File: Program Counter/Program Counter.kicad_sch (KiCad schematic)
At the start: 48 parts, among them J1 Conn_01x03_Pin, J4 Conn_01x08_Pin, J5 Conn_01x08_Pin, U1 74LS161, U2 74LS161, U3 74LS161, U4 74LS161

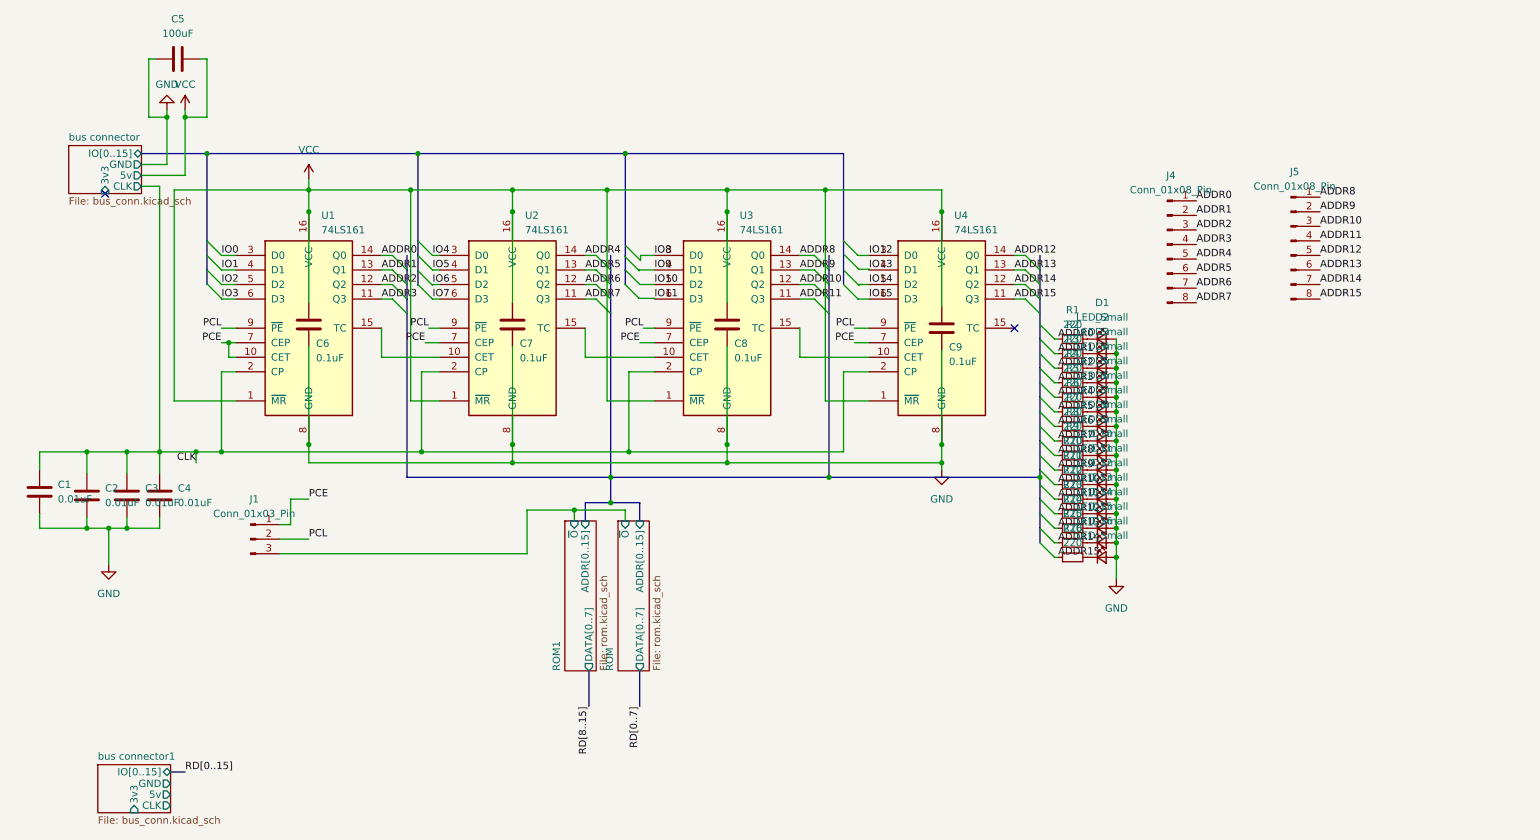
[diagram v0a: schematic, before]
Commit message: Overhauled program counter schematic
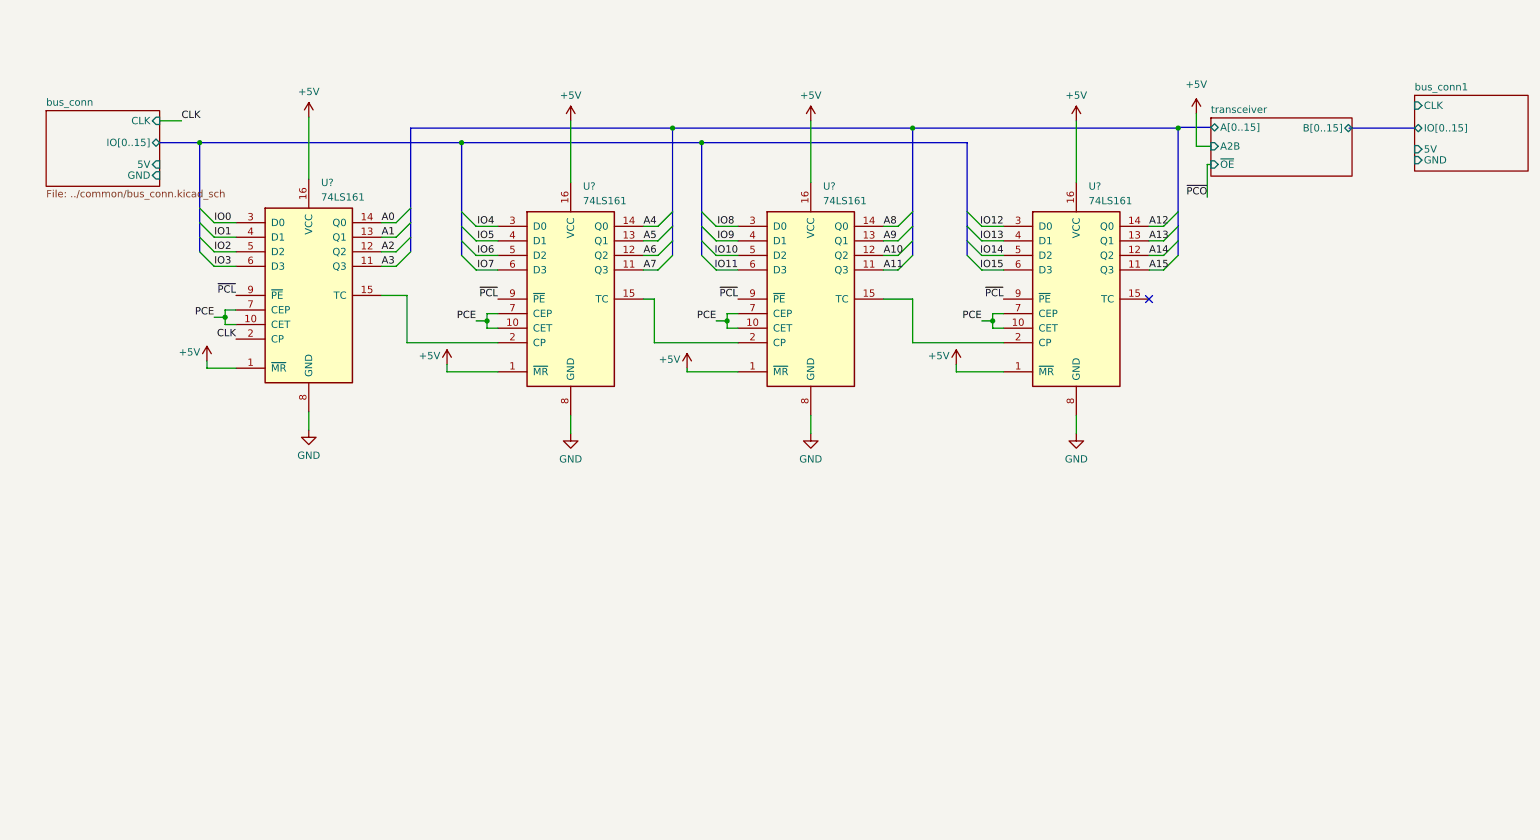
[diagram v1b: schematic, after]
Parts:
- removed C1, C2, C3, C4: 0.01uF, Capacitor_SMD:C_0603_1608Metric, symbol Device:C
- removed C5: 100uF, Capacitor_SMD:CP_Elec_5x5.3, symbol Device:C
- removed C6, C7, C8, C9: 0.1uF, Capacitor_SMD:C_0603_1608Metric, symbol Device:C
- removed D1, D10, D11, D12, D13, D14, D15, D16, D2, D3, D4, D5, D6, D7, D8, D9: LED_Small, LED_SMD:LED_0603_1608Metric, symbol Device:LED_Small
- removed J1: Conn_01x03_Pin, Connector_PinHeader_2.54mm:PinHeader_1x03_P2.54mm_Vertical, symbol Connector:Conn_01x03_Pin
- removed J4, J5: Conn_01x08_Pin, Connector_PinHeader_2.54mm:PinHeader_1x08_P2.54mm_Vertical, symbol Connector:Conn_01x08_Pin
- removed R1, R10, R11, R12, R13, R14, R15, R16, R2, R3, R4, R5, R6, R7, R8, R9: 220, Resistor_SMD:R_0603_1608Metric, symbol Device:R_Small
- removed U1, U2, U3, U4: 74LS161, Package_SO:SO-16_3.9x9.9mm_P1.27mm, symbol 74xx:74LS161
- added U? (x4): 74LS161, symbol 74xx:74LS161
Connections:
- net CLK: now also U?.2 (CP)
- net GND: now also U?.8 (GND), U?.8 (GND), U?.8 (GND), U?.8 (GND)
- net IO0: now also U?.3 (D0)
- net IO1: now also U?.4 (D1)
- net IO10: now also U?.5 (D2)
- net IO11: now also U?.6 (D3)
- net IO12: now also U?.3 (D0)
- net IO13: now also U?.4 (D1)
- net IO14: now also U?.5 (D2)
- net IO15: now also U?.6 (D3)
- net IO2: now also U?.5 (D2)
- net IO3: now also U?.6 (D3)
- net IO4: now also U?.3 (D0)
- net IO5: now also U?.4 (D1)
- net IO6: now also U?.5 (D2)
- net IO7: now also U?.6 (D3)
- net IO8: now also U?.3 (D0)
- net IO9: now also U?.4 (D1)
- net PCE: now also U?.10 (CET), U?.10 (CET), U?.10 (CET), U?.10 (CET), U?.7 (CEP), U?.7 (CEP), U?.7 (CEP), U?.7 (CEP)
- new net: U?.15 (TC), U?.2 (CP) (x3)
- new net +5V: U?.1 (~{MR}), U?.1 (~{MR}), U?.1 (~{MR}), U?.1 (~{MR}), U?.16 (VCC), U?.16 (VCC), U?.16 (VCC), U?.16 (VCC)
- new net A0: U?.14 (Q0)
- new net A1: U?.13 (Q1)
- new net A10: U?.12 (Q2)
- new net A11: U?.11 (Q3)
- new net A12: U?.14 (Q0)
- new net A13: U?.13 (Q1)
- new net A14: U?.12 (Q2)
- new net A15: U?.11 (Q3)
- new net A2: U?.12 (Q2)
- new net A3: U?.11 (Q3)
- new net A4: U?.14 (Q0)
- new net A5: U?.13 (Q1)
- new net A6: U?.12 (Q2)
- new net A7: U?.11 (Q3)
- new net A8: U?.14 (Q0)
- new net A9: U?.13 (Q1)
- new net ~{PCL}: U?.9 (~{PE}), U?.9 (~{PE}), U?.9 (~{PE}), U?.9 (~{PE})
- no-connect marks 2 -> 1
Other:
- removed sheet ROM
- removed sheet ROM1
- removed sheet bus connector
- removed sheet bus connector1
- added sheet bus_conn (../common/bus_conn.kicad_sch)
- added sheet bus_conn1 (../common/bus_conn.kicad_sch)
- added sheet transceiver (../common/tri-state buffer16.kicad_sch)

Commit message: Added program counter PCB
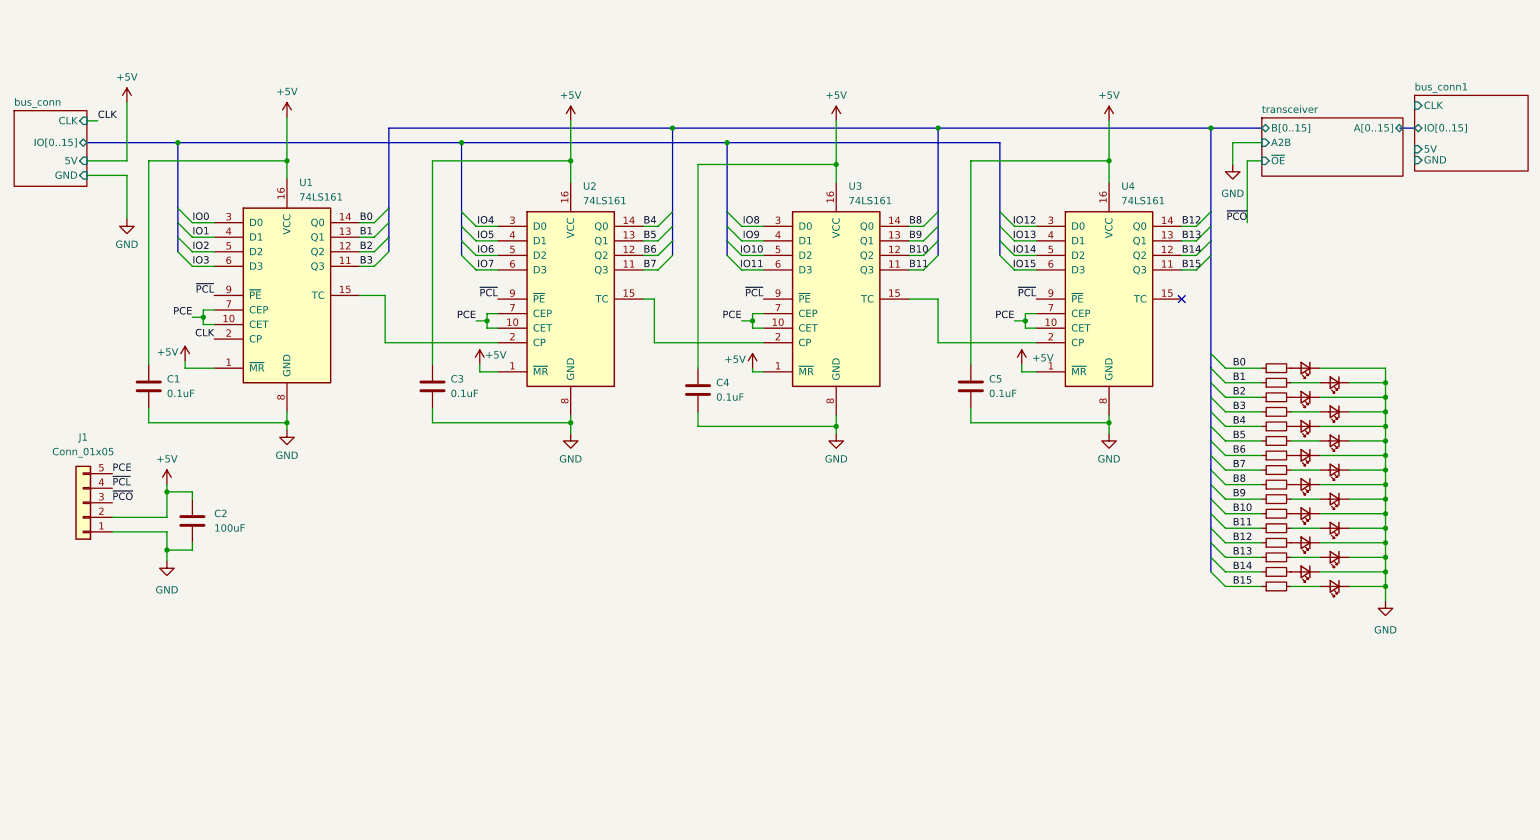
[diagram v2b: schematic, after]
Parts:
- added C1, C3, C4, C5: 0.1uF, Capacitor_SMD:C_0603_1608Metric, symbol Device:C
- added C2: 100uF, Capacitor_SMD:CP_Elec_5x5.3, symbol Device:C
- added D1, D10, D11, D12, D13, D14, D15, D16, D2, D3, D4, D5, D6, D7, D8, D9: LED_Small, LED_SMD:LED_0603_1608Metric, symbol Device:LED_Small
- added J1: Conn_01x05, Connector_PinHeader_2.54mm:PinHeader_1x05_P2.54mm_Vertical, symbol Connector_Generic:Conn_01x05
- added R10, R11, R12, R13, R14, R15, R16, R17, R2, R3, R4, R5, R6, R7, R8, R9: 220, Resistor_SMD:R_0603_1608Metric, symbol Device:R_Small
- U1, U2, U3, U4: renamed from U?; footprint (none) -> Package_SO:SOIC-16_4.55x10.3mm_P1.27mm
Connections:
- net +5V: now also C1.1, C2.1, C3.1, C4.1, C5.1, J1.2 (Pin_2)
- net GND: now also C1.2, C2.2, C3.2, C4.2, C5.2, D1.1 (K), D10.1 (K), D11.1 (K), D12.1 (K), D13.1 (K), D14.1 (K), D15.1 (K), D16.1 (K), D2.1 (K), D3.1 (K), D4.1 (K), D5.1 (K), D6.1 (K), D7.1 (K), D8.1 (K), D9.1 (K), J1.1 (Pin_1)
- net PCE: now also J1.5 (Pin_5)
- net ~{PCL}: now also J1.4 (Pin_4)
- net ~{PCO}: now also J1.3 (Pin_3)
- net A0 renamed B0
- net B0: now also R2.1
- net A1 renamed B1
- net B1: now also R3.1
- net A10 renamed B10
- net B10: now also R12.1
- net A11 renamed B11
- net B11: now also R13.1
- net A12 renamed B12
- net B12: now also R14.1
- net A13 renamed B13
- net B13: now also R15.1
- net A14 renamed B14
- net B14: now also R16.1
- net A15 renamed B15
- net B15: now also R17.1
- net A2 renamed B2
- net B2: now also R4.1
- net A3 renamed B3
- net B3: now also R5.1
- net A4 renamed B4
- net B4: now also R6.1
- net A5 renamed B5
- net B5: now also R7.1
- net A6 renamed B6
- net B6: now also R8.1
- net A7 renamed B7
- net B7: now also R9.1
- net A8 renamed B8
- net B8: now also R10.1
- net A9 renamed B9
- net B9: now also R11.1
- new net: D12.2 (A), R9.2
- new net: D5.2 (A), R10.2
- new net: D6.2 (A), R12.2
- new net: D2.2 (A), R4.2
- new net: D4.2 (A), R8.2
- new net: D14.2 (A), R13.2
- new net: D3.2 (A), R6.2
- new net: D7.2 (A), R14.2
- new net: D10.2 (A), R5.2
- new net: D9.2 (A), R3.2
- new net: D11.2 (A), R7.2
- new net: D1.2 (A), R2.2
- new net: D15.2 (A), R15.2
- new net: D13.2 (A), R11.2
- new net: D8.2 (A), R16.2
- new net: D16.2 (A), R17.2
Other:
- moved on the sheet: U1, U3, U4

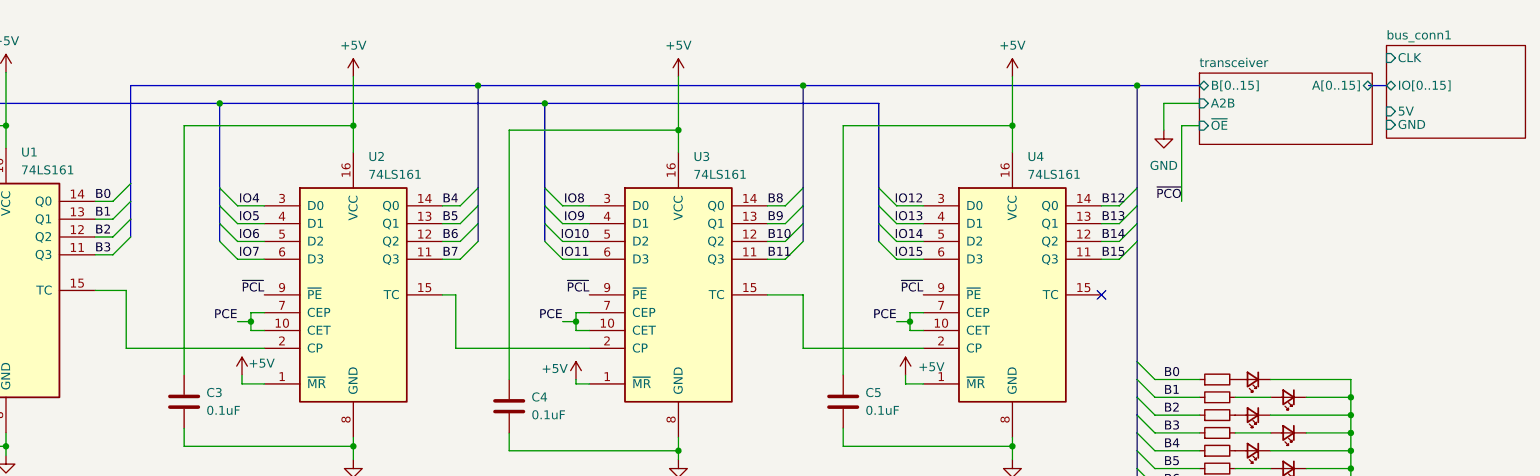
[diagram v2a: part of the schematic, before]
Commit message: Updated silkscreen and cascade wiring program counter
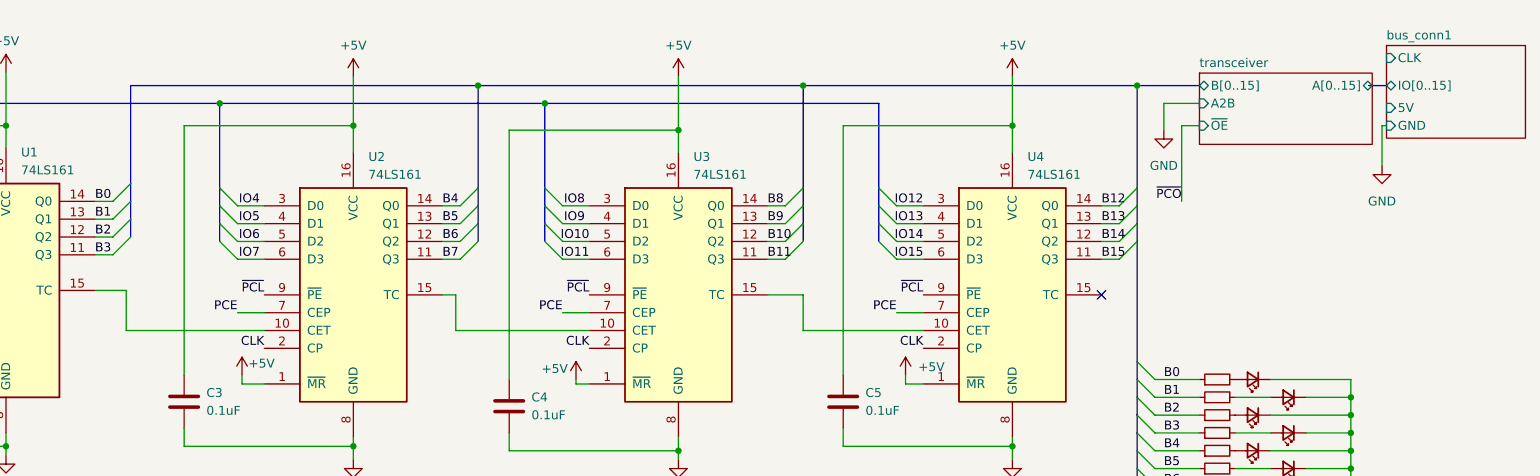
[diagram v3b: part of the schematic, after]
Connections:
- net CLK: now also U2.2 (CP), U3.2 (CP), U4.2 (CP)
- net PCE: no longer U2.10 (CET), U3.10 (CET), U4.10 (CET)
- net at U3.15 (TC): now also U4.10 (CET); no longer U4.2 (CP)
- net at U2.15 (TC): now also U3.10 (CET); no longer U3.2 (CP)
- net at U1.15 (TC): now also U2.10 (CET); no longer U2.2 (CP)
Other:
- title: (none) -> AOS16 Program Counter
